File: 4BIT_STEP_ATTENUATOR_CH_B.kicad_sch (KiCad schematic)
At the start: 7 parts, among them IC801 ${DEVICE}

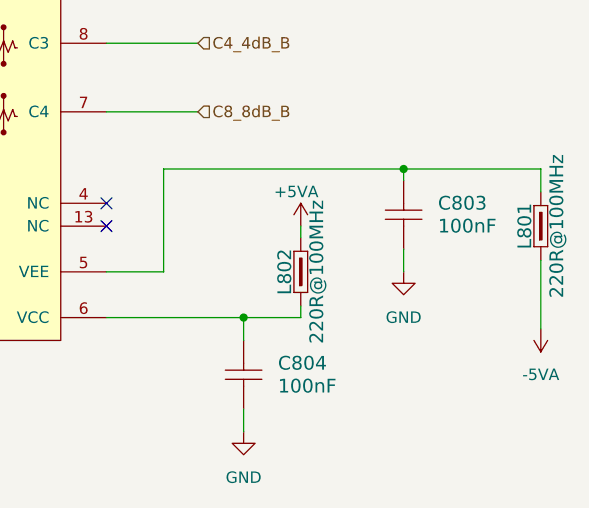
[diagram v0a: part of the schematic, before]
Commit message: Rerouted PCB Logic part
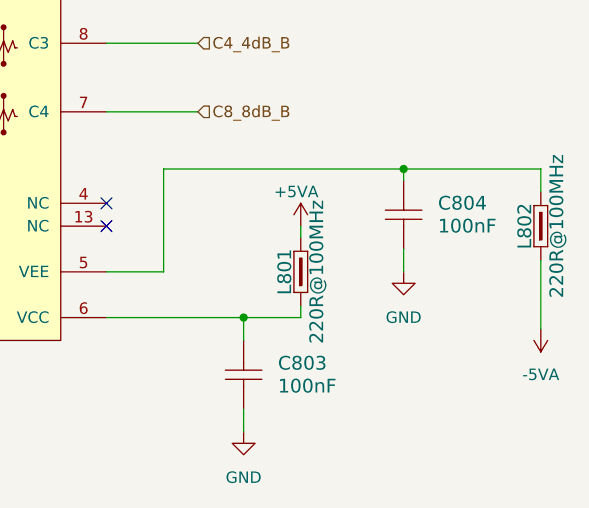
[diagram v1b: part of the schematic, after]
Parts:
- renumbered C804 to C803, C803 to C804, L802 to L801, L801 to L802
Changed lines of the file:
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@@
 		(dnp no)
 		(fields_autoplaced yes)
-		(property "Reference" "#PWR0804"
+		(property "Reference" "#PWR0805"
 			(at 213.36 109.22 0)
 			(effects
@@
 			(project "8CH_Analog_Front_END"
 				(path "/41597329-5145-432a-9041-5bc2cec82d9b/e0337a1b-c397-4f99-b607-786eab07764a/a80631d7-e4a9-40d1-806c-5d968f53661a"
-					(reference "#PWR0804")
+					(reference "#PWR0805")
 					(unit 1)
 				)
@@
 		(dnp no)
 		(fields_autoplaced yes)
-		(property "Reference" "#PWR0802"
+		(property "Reference" "#PWR0804"
 			(at 198.12 113.03 0)
 			(effects
@@
 			(project "8CH_Analog_Front_END"
 				(path "/41597329-5145-432a-9041-5bc2cec82d9b/e0337a1b-c397-4f99-b607-786eab07764a/a80631d7-e4a9-40d1-806c-5d968f53661a"
-					(reference "#PWR0802")
+					(reference "#PWR0804")
 					(unit 1)
 				)
@@
 		(dnp no)
 		(fields_autoplaced yes)
-		(property "Reference" "C804"
+		(property "Reference" "C803"
 			(at 184.15 116.8399 90)
 			(effects
@@
 			(project "8CH_Analog_Front_END"
 				(path "/41597329-5145-432a-9041-5bc2cec82d9b/e0337a1b-c397-4f99-b607-786eab07764a/a80631d7-e4a9-40d1-806c-5d968f53661a"
-					(reference "C804")
+					(reference "C803")
 					(unit 1)
 				)
@@
 		(on_board yes)
 		(dnp no)
-		(property "Reference" "#PWR0801"
+		(property "Reference" "#PWR0803"
 			(at 186.69 105.41 0)
 			(effects
@@
 			(project "8CH_Analog_Front_END"
 				(path "/41597329-5145-432a-9041-5bc2cec82d9b/e0337a1b-c397-4f99-b607-786eab07764a/a80631d7-e4a9-40d1-806c-5d968f53661a"
-					(reference "#PWR0801")
+					(reference "#PWR0803")
 					(unit 1)
 				)
@@
 		(on_board yes)
 		(dnp no)
-		(property "Reference" "L802"
+		(property "Reference" "L801"
 			(at 184.912 106.68 0)
 			(effects
@@
 			(project "8CH_Analog_Front_END"
 				(path "/41597329-5145-432a-9041-5bc2cec82d9b/e0337a1b-c397-4f99-b607-786eab07764a/a80631d7-e4a9-40d1-806c-5d968f53661a"
-					(reference "L802")
+					(reference "L801")
 					(unit 1)
 				)
@@
 		(on_board yes)
 		(dnp no)
-		(property "Reference" "L801"
+		(property "Reference" "L802"
 			(at 211.582 101.6 0)
 			(effects
@@
 			(project "8CH_Analog_Front_END"
 				(path "/41597329-5145-432a-9041-5bc2cec82d9b/e0337a1b-c397-4f99-b607-786eab07764a/a80631d7-e4a9-40d1-806c-5d968f53661a"
-					(reference "L801")
+					(reference "L802")
 					(unit 1)
 				)
@@
 		(dnp no)
 		(fields_autoplaced yes)
-		(property "Reference" "C803"
+		(property "Reference" "C804"
 			(at 201.93 99.0599 90)
 			(effects
@@
 			(project "8CH_Analog_Front_END"
 				(path "/41597329-5145-432a-9041-5bc2cec82d9b/e0337a1b-c397-4f99-b607-786eab07764a/a80631d7-e4a9-40d1-806c-5d968f53661a"
-					(reference "C803")
+					(reference "C804")
 					(unit 1)
 				)
@@
 		(dnp no)
 		(fields_autoplaced yes)
-		(property "Reference" "#PWR0803"
+		(property "Reference" "#PWR0801"
 			(at 137.16 130.81 0)
 			(effects
@@
 			(project "8CH_Analog_Front_END"
 				(path "/41597329-5145-432a-9041-5bc2cec82d9b/e0337a1b-c397-4f99-b607-786eab07764a/a80631d7-e4a9-40d1-806c-5d968f53661a"
-					(reference "#PWR0803")
+					(reference "#PWR0801")
 					(unit 1)
 				)
@@
 		(dnp no)
 		(fields_autoplaced yes)
-		(property "Reference" "#PWR0805"
+		(property "Reference" "#PWR0802"
 			(at 180.34 130.81 0)
 			(effects
@@
 			(project "8CH_Analog_Front_END"
 				(path "/41597329-5145-432a-9041-5bc2cec82d9b/e0337a1b-c397-4f99-b607-786eab07764a/a80631d7-e4a9-40d1-806c-5d968f53661a"
-					(reference "#PWR0805")
+					(reference "#PWR0802")
 					(unit 1)
 				)
